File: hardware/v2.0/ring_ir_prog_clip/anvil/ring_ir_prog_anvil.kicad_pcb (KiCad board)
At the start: 2 copper layers, 22.5 x 31 mm, 2 parts, among them J1 GND_lead_to_probe, P8 GND anvil (TP8 bar)

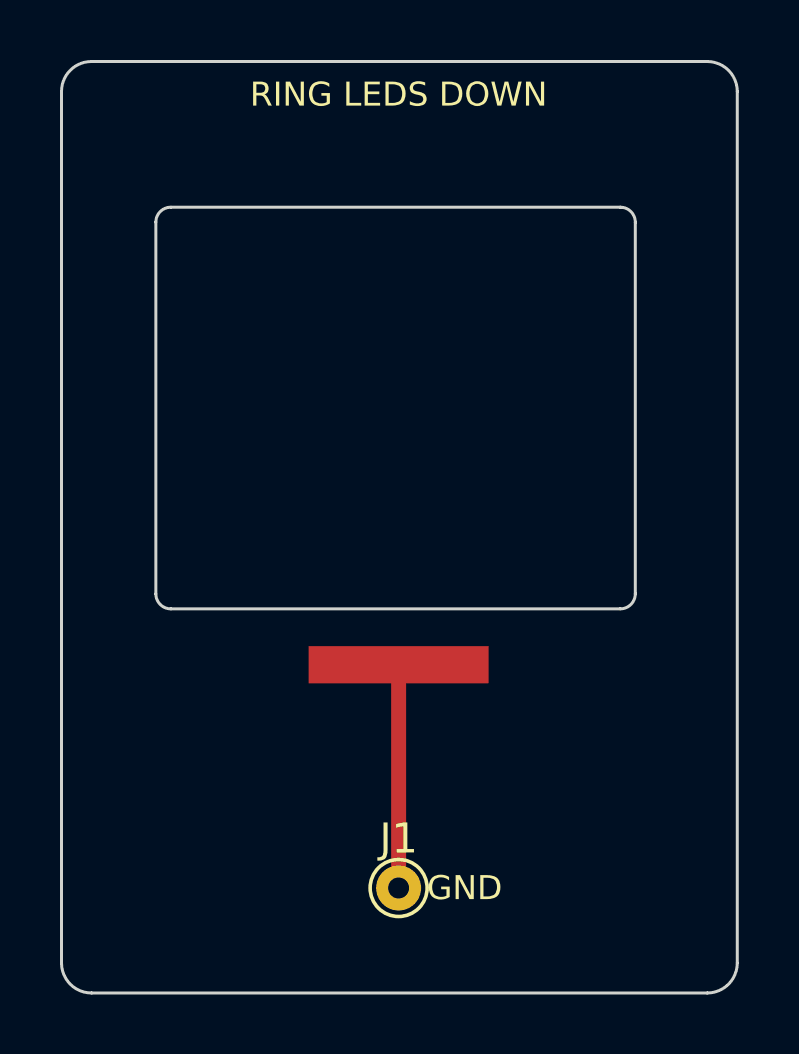
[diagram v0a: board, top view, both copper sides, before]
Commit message: IR prog clip: estimated clip dimensions and FreeCAD virtual fit check
Co-authored-by: Copilot <223556219+Copilot@users.noreply.github.com>
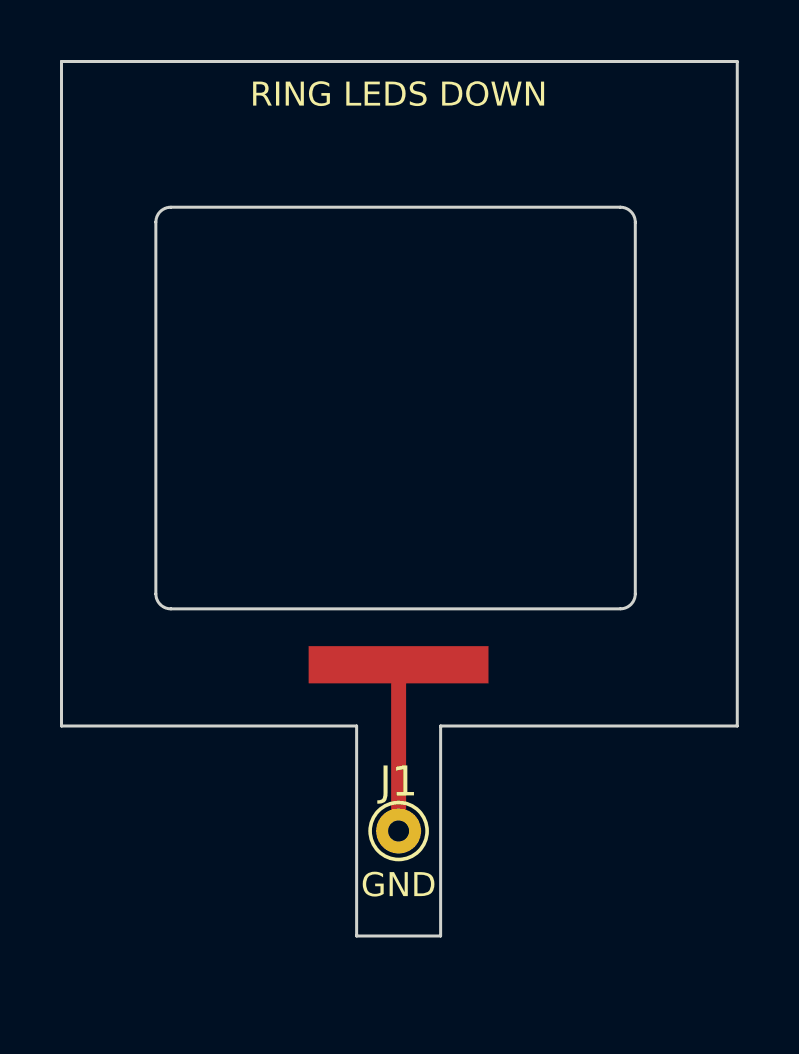
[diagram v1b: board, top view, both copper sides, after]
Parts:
- moved J1 1.90 mm to (150.0, 109.0)
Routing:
- net /GND: track 7.44 -> 5.54 mm
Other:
- board size 22.5 x 31 mm -> 22.5 x 29.2 mm
- board text added: "IR ANVIL - TAPE TO RISER"
- board text removed: "IR ANVIL - TAPE TO LOWER JAW"
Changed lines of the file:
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@@
 		)
+	)
+	(footprint "ring_ir_prog_clip:GND_Anvil_Pad"
+		(layer "F.Cu")
+		(at 150 103.4097)
+		(descr "Exposed flat GND contact under the ring_pcb_IR front GND bar. Generated from the target board")
+		(tags "anvil contact ground")
+		(property "Reference" "P8"
+			(at 0 -1.12 0)
+			(layer "F.Fab")
+			(effects
+				(font
+					(size 0.5 0.5)
+					(thickness 0.08)
+				)
+			)
+		)
+		(property "Value" "GND anvil (TP8 bar)"
+			(at 0 1.12 0)
+			(layer "F.Fab")
+			(effects
+				(font
+					(size 0.5 0.5)
+					(thickness 0.08)
+				)
+			)
+		)
+		(property "Datasheet" ""
+			(at 0 0 0)
+			(layer "F.Fab")
+			(hide yes)
+			(effects
+				(font
+					(size 1.27 1.27)
+				)
+			)
+		)
+		(property "Description" ""
+			(at 0 0 0)
+			(layer "F.Fab")
+			(hide yes)
+			(effects
+				(font
+					(size 1.27 1.27)
+				)
+			)
+		)
+		(sheetfile "ring_ir_prog_anvil.kicad_sch")
+		(attr smd)
+		(duplicate_pad_numbers_are_jumpers no)
+		(fp_rect
+			(start -3.1 -0.72)
+			(end 3.1 0.72)
+			(stroke
+				(width 0.05)
+				(type solid)
+			)
+			(fill no)
+			(layer "F.CrtYd")
+		)
+		(pad "1" smd rect
+			(at 0 0)
+			(size 6 1.241)
+			(layers "F.Cu" "F.Mask")
+			(net "/GND")
+		)
+		(embedded_fonts no)
 	)
 	(footprint "TestPoint:TestPoint_THTPad_D1.5mm_Drill0.7mm"
 		(layer "F.Cu")
-		(at 150 110.8514)
+		(at 150 108.9514)
 		(descr "THT pad as test Point, diameter 1.5mm, hole diameter 0.7mm")
 		(tags "test point THT pad")
@@
 		(embedded_fonts no)
 	)
-	(footprint "ring_ir_prog_clip:GND_Anvil_Pad"
-		(layer "F.Cu")
-		(at 150 103.4097)
-		(descr "Exposed flat GND contact under the ring_pcb_IR front GND bar. Generated from the target board")
-		(tags "anvil contact ground")
-		(property "Reference" "P8"
-			(at 0 -1.12 0)
-			(layer "F.Fab")
-			(effects
-				(font
-					(size 0.5 0.5)
-					(thickness 0.08)
-				)
-			)
-		)
-		(property "Value" "GND anvil (TP8 bar)"
-			(at 0 1.12 0)
-			(layer "F.Fab")
-			(effects
-				(font
-					(size 0.5 0.5)
-					(thickness 0.08)
-				)
-			)
-		)
-		(property "Datasheet" ""
-			(at 0 0 0)
-			(layer "F.Fab")
-			(hide yes)
-			(effects
-				(font
-					(size 1.27 1.27)
-				)
-			)
-		)
-		(property "Description" ""
-			(at 0 0 0)
-			(layer "F.Fab")
-			(hide yes)
-			(effects
-				(font
-					(size 1.27 1.27)
-				)
-			)
-		)
-		(sheetfile "ring_ir_prog_anvil.kicad_sch")
-		(attr smd)
-		(duplicate_pad_numbers_are_jumpers no)
-		(fp_rect
-			(start -3.1 -0.72)
-			(end 3.1 0.72)
-			(stroke
-				(width 0.05)
-				(type solid)
-			)
-			(fill no)
-			(layer "F.CrtYd")
-		)
-		(pad "1" smd rect
-			(at 0 0)
-			(size 6 1.241)
-			(layers "F.Cu" "F.Mask")
-			(net "/GND")
-		)
-		(embedded_fonts no)
-	)
-	(gr_arc
-		(start 138.7624 84.3014)
-		(mid 139.055293 83.594293)
-		(end 139.7624 83.3014)
-		(stroke
-			(width 0.1)
-			(type default)
-		)
-		(layer "Edge.Cuts")
-	)
-	(gr_line
-		(start 138.7624 113.3514)
-		(end 138.7624 84.3014)
-		(stroke
-			(width 0.1)
-			(type default)
-		)
-		(layer "Edge.Cuts")
-	)
-	(gr_line
-		(start 139.7624 83.3014)
-		(end 160.2884 83.3014)
-		(stroke
-			(width 0.1)
-			(type default)
-		)
-		(layer "Edge.Cuts")
-	)
-	(gr_arc
-		(start 139.7624 114.3514)
-		(mid 139.055293 114.058506)
-		(end 138.7624 113.3514)
+	(gr_line
+		(start 138.7624 83.3014)
+		(end 161.2884 83.3014)
+		(stroke
+			(width 0.1)
+			(type default)
+		)
+		(layer "Edge.Cuts")
+	)
+	(gr_line
+		(start 138.7624 105.4514)
+		(end 138.7624 83.3014)
 		(stroke
 			(width 0.1)
@@
 		(layer "Edge.Cuts")
 	)
+	(gr_line
+		(start 148.6 105.4514)
+		(end 138.7624 105.4514)
+		(stroke
+			(width 0.1)
+			(type default)
+		)
+		(layer "Edge.Cuts")
+	)
+	(gr_line
+		(start 148.6 112.4514)
+		(end 148.6 105.4514)
+		(stroke
+			(width 0.1)
+			(type default)
+		)
+		(layer "Edge.Cuts")
+	)
+	(gr_line
+		(start 151.4 105.4514)
+		(end 151.4 112.4514)
+		(stroke
+			(width 0.1)
+			(type default)
+		)
+		(layer "Edge.Cuts")
+	)
+	(gr_line
+		(start 151.4 112.4514)
+		(end 148.6 112.4514)
+		(stroke
+			(width 0.1)
+			(type default)
+		)
+		(layer "Edge.Cuts")
+	)
 	(gr_arc
 		(start 157.3894 88.1584)
@@
 		(layer "Edge.Cuts")
 	)
-	(gr_arc
-		(start 160.2884 83.3014)
-		(mid 160.995506 83.594293)
-		(end 161.2884 84.3014)
-		(stroke
-			(width 0.1)
-			(type default)
-		)
-		(layer "Edge.Cuts")
-	)
-	(gr_line
-		(start 160.2884 114.3514)
-		(end 139.7624 114.3514)
-		(stroke
-			(width 0.1)
-			(type default)
-		)
-		(layer "Edge.Cuts")
-	)
-	(gr_line
-		(start 161.2884 84.3014)
-		(end 161.2884 113.3514)
-		(stroke
-			(width 0.1)
-			(type default)
-		)
-		(layer "Edge.Cuts")
-	)
-	(gr_arc
-		(start 161.2884 113.3514)
-		(mid 160.995506 114.058506)
-		(end 160.2884 114.3514)
+	(gr_line
+		(start 161.2884 83.3014)
+		(end 161.2884 105.4514)
+		(stroke
+			(width 0.1)
+			(type default)
+		)
+		(layer "Edge.Cuts")
+	)
+	(gr_line
+		(start 161.2884 105.4514)
+		(end 151.4 105.4514)
 		(stroke
 			(width 0.1)
@@
 	)
 	(gr_text "GND"
-		(at 152.2 110.8514 0)
+		(at 150 110.7514 0)
 		(layer "F.SilkS")
 		(effects
@@
 		)
 	)
-	(gr_text "IR ANVIL - TAPE TO LOWER JAW"
-		(at 150 113.1514 0)
+	(gr_text "IR ANVIL - TAPE TO RISER"
+		(at 150 84.4014 0)
 		(layer "B.SilkS")
 		(effects
@@
 	(segment
 		(start 150 103.4097)
-		(end 150 110.8514)
+		(end 150 108.9514)
 		(width 0.5)
 		(layer "F.Cu")
